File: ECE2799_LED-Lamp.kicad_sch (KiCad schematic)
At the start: 0 parts

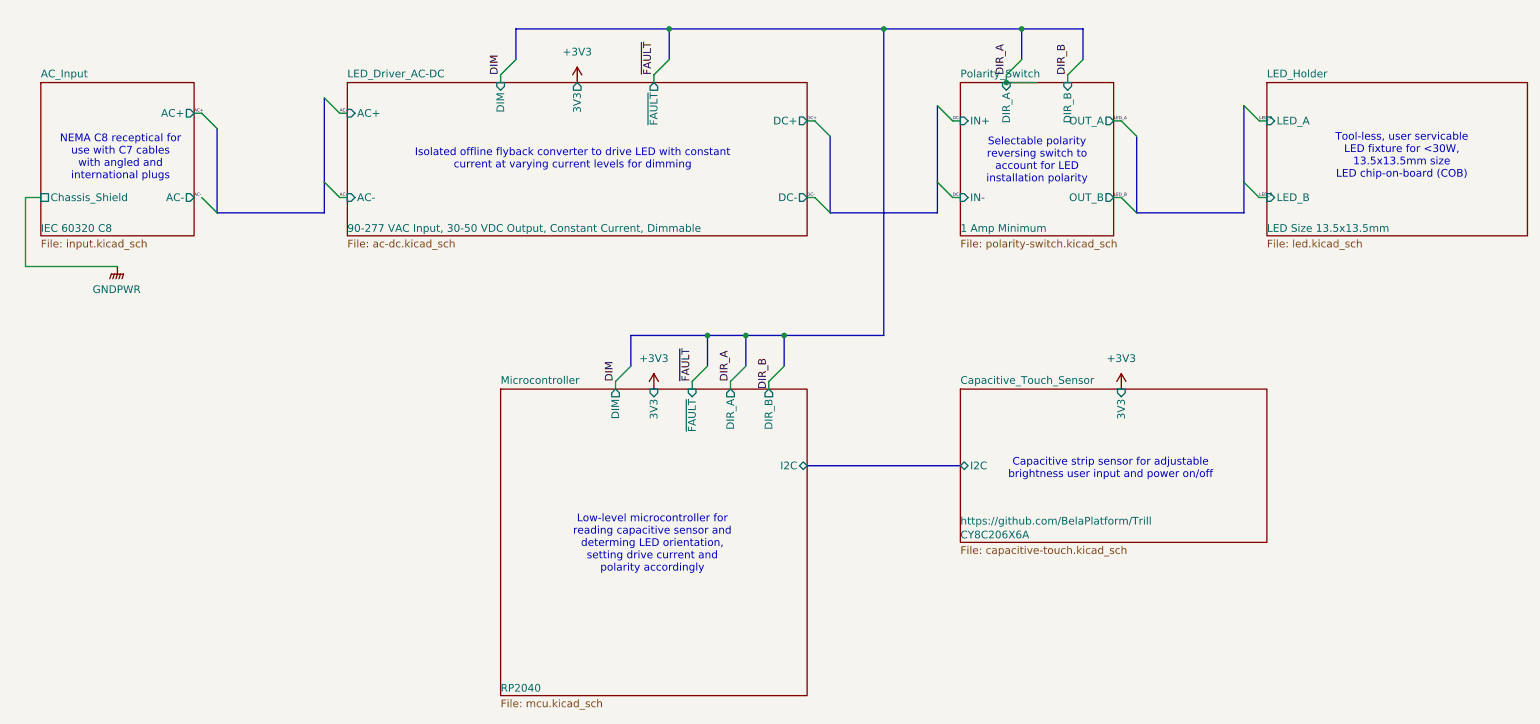
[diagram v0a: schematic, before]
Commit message: updated components
New ganfet selected and further work developing the rp2040 microcontroller circuit
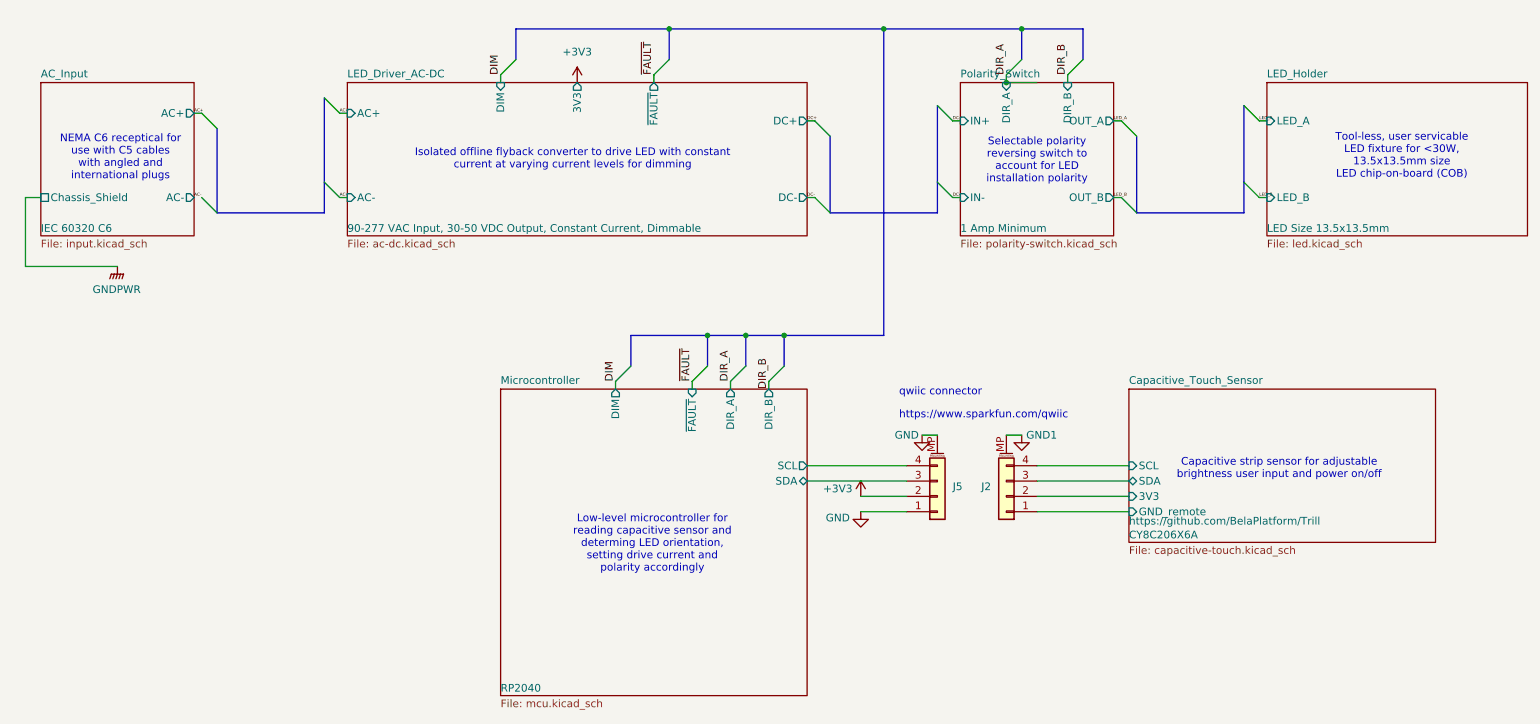
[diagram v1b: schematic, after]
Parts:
- added J2, J5: Conn_01x04_MountingPin, TRILL:qwiic_horizontal_SMD, symbol Connector_Generic_MountingPin:Conn_01x04_MountingPin
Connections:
- net +3V3: now also J5.2 (Pin_2)
- new net Capacitive_Touch_Sensor/3V3: J2.2 (Pin_2)
- new net Capacitive_Touch_Sensor/GND_remote: J2.1 (Pin_1)
- new net Capacitive_Touch_Sensor/SCL: J2.4 (Pin_4)
- new net Capacitive_Touch_Sensor/SDA: J2.3 (Pin_3)
- new net GND: J5.1 (Pin_1), J5.MP (MountPin)
- new net GND1: J2.MP (MountPin)
- new net Microcontroller/SCL: J5.4 (Pin_4)
- new net Microcontroller/SDA: J5.3 (Pin_3)
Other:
- sheet Capacitive_Touch_Sensor ports: added GND_remote, SCL, SDA; removed I2C
- sheet Microcontroller ports: added SCL, SDA; removed 3V3, I2C
- note added: "NEMA C6 receptical for use with C5 cables with angled and international plugs"
- note added: "https://www.sparkfun.com/qwiic"
- note added: "qwiic connector"
- note removed: "NEMA C8 receptical for use with C7 cables with angled and international plugs"

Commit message: production design files
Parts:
- added H1: MountingHole_Pad, MountingHole:MountingHole_3.2mm_M3_Pad, symbol Mechanical:MountingHole_Pad
- added H2: MountingHole, MountingHole:MountingHole_3.2mm_M3, symbol Mechanical:MountingHole
- J2, J5: Part Number (none) -> PRT-14417-ND
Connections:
- net GNDPWR: now also H1.1
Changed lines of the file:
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@@
+	)
+	(symbol
+		(lib_id "Mechanical:MountingHole_Pad")
+		(at 25.4 170.18 0)
+		(unit 1)
+		(exclude_from_sim yes)
+		(in_bom no)
+		(on_board yes)
+		(dnp no)
+		(fields_autoplaced yes)
+		(property "Reference" "H1"
+			(at 27.94 167.6399 0)
+			(effects
+				(font
+					(size 1.27 1.27)
+				)
+				(justify left)
+			)
+		)
+		(property "Value" "MountingHole_Pad"
+			(at 27.94 170.1799 0)
+			(effects
+				(font
+					(size 1.27 1.27)
+				)
+				(justify left)
+				(hide yes)
+			)
+		)
+		(property "Footprint" "MountingHole:MountingHole_3.2mm_M3_Pad"
+			(at 25.4 170.18 0)
+			(effects
+				(font
+					(size 1.27 1.27)
+				)
+				(hide yes)
+			)
+		)
+		(property "Datasheet" "~"
+			(at 25.4 170.18 0)
+			(effects
+				(font
+					(size 1.27 1.27)
+				)
+				(hide yes)
+			)
+		)
+		(property "Description" "Mounting Hole with connection"
+			(at 25.4 170.18 0)
+			(effects
+				(font
+					(size 1.27 1.27)
+				)
+				(hide yes)
+			)
+		)
+		(pin "1"
+		)
+		(instances
+			(project ""
+				(path "/c27c9155-8dca-4b9f-ac37-1fd4cce6afa0"
+					(reference "H1")
+					(unit 1)
+				)
+			)
+		)
 	)
 	(symbol
@@
 				(path "/c27c9155-8dca-4b9f-ac37-1fd4cce6afa0"
 					(reference "#PWR04")
+					(unit 1)
+				)
+			)
+		)
+	)
+	(symbol
+		(lib_id "Mechanical:MountingHole")
+		(at 34.29 168.91 0)
+		(unit 1)
+		(exclude_from_sim yes)
+		(in_bom no)
+		(on_board yes)
+		(dnp no)
+		(fields_autoplaced yes)
+		(property "Reference" "H2"
+			(at 36.83 167.6399 0)
+			(effects
+				(font
+					(size 1.27 1.27)
+				)
+				(justify left)
+			)
+		)
+		(property "Value" "MountingHole"
+			(at 36.83 170.1799 0)
+			(effects
+				(font
+					(size 1.27 1.27)
+				)
+				(justify left)
+				(hide yes)
+			)
+		)
+		(property "Footprint" "MountingHole:MountingHole_3.2mm_M3"
+			(at 34.29 168.91 0)
+			(effects
+				(font
+					(size 1.27 1.27)
+				)
+				(hide yes)
+			)
+		)
+		(property "Datasheet" "~"
+			(at 34.29 168.91 0)
+			(effects
+				(font
+					(size 1.27 1.27)
+				)
+				(hide yes)
+			)
+		)
+		(property "Description" "Mounting Hole without connection"
+			(at 34.29 168.91 0)
+			(effects
+				(font
+					(size 1.27 1.27)
+				)
+				(hide yes)
+			)
+		)
+		(instances
+			(project ""
+				(path "/c27c9155-8dca-4b9f-ac37-1fd4cce6afa0"
+					(reference "H2")
 					(unit 1)
 				)
@@
 			)
 		)
-		(property "Datasheet" "~"
+		(property "Datasheet" "https://www.sparkfun.com/qwiic"
 			(at 173.99 144.78 0)
 			(effects
@@
 			)
 		)
-		(property "Part Number" ""
+		(property "Part Number" "PRT-14417-ND"
 			(at 173.99 144.78 0)
 			(effects
@@
 					(size 1.27 1.27)
 				)
+				(hide yes)
 			)
 		)
@@
 			)
 		)
-		(property "Datasheet" "~"
+		(property "Datasheet" "https://www.sparkfun.com/qwiic"
 			(at 185.42 144.78 0)
 			(effects
@@
 			)
 		)
-		(property "Part Number" ""
+		(property "Part Number" "PRT-14417-ND"
 			(at 185.42 144.78 0)
 			(effects
@@
 					(size 1.27 1.27)
 				)
+				(hide yes)
 			)
 		)
@@
 					(unit 1)
 				)
+			)
+		)
+	)
+	(symbol
+		(lib_id "power:GNDPWR")
+		(at 25.4 172.72 0)
+		(unit 1)
+		(exclude_from_sim no)
+		(in_bom yes)
+		(on_board yes)
+		(dnp no)
+		(fields_autoplaced yes)
+		(property "Reference" "#PWR015"
+			(at 25.4 177.8 0)
+			(effects
+				(font
+					(size 1.27 1.27)
+				)
+				(hide yes)
+			)
+		)
+		(property "Value" "GNDPWR"
+			(at 25.273 176.53 0)
+			(effects
+				(font
+					(size 1.27 1.27)
+				)
+			)
+		)
+		(property "Footprint" ""
+			(at 25.4 173.99 0)
+			(effects
+				(font
+					(size 1.27 1.27)
+				)
+				(hide yes)
+			)
+		)
+		(property "Datasheet" ""
+			(at 25.4 173.99 0)
+			(effects
+				(font
+					(size 1.27 1.27)
+				)
+				(hide yes)
+			)
+		)
+		(property "Description" "Power symbol creates a global label with name \"GNDPWR\" , global ground"
+			(at 25.4 172.72 0)
+			(effects
+				(font
+					(size 1.27 1.27)
+				)
+				(hide yes)
+			)
+		)
+		(pin "1"
+		)
+		(instances
+			(project "ECE2799_LED-Lamp"
+				(path "/c27c9155-8dca-4b9f-ac37-1fd4cce6afa0"
+					(reference "#PWR015")
+					(unit 1)
+				)
